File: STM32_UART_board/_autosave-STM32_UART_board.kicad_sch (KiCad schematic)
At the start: 35 parts, among them J1 SWD, J2 Scooter, J3 Conn_01x10, Q1 AO4612_C4748739, SW1 SW_Push, SW2 SW_Push, U1 BAS70-05, U2 LM2574HVM-5, U3 AZ1117-3.3, U4 STM32C011F6Px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

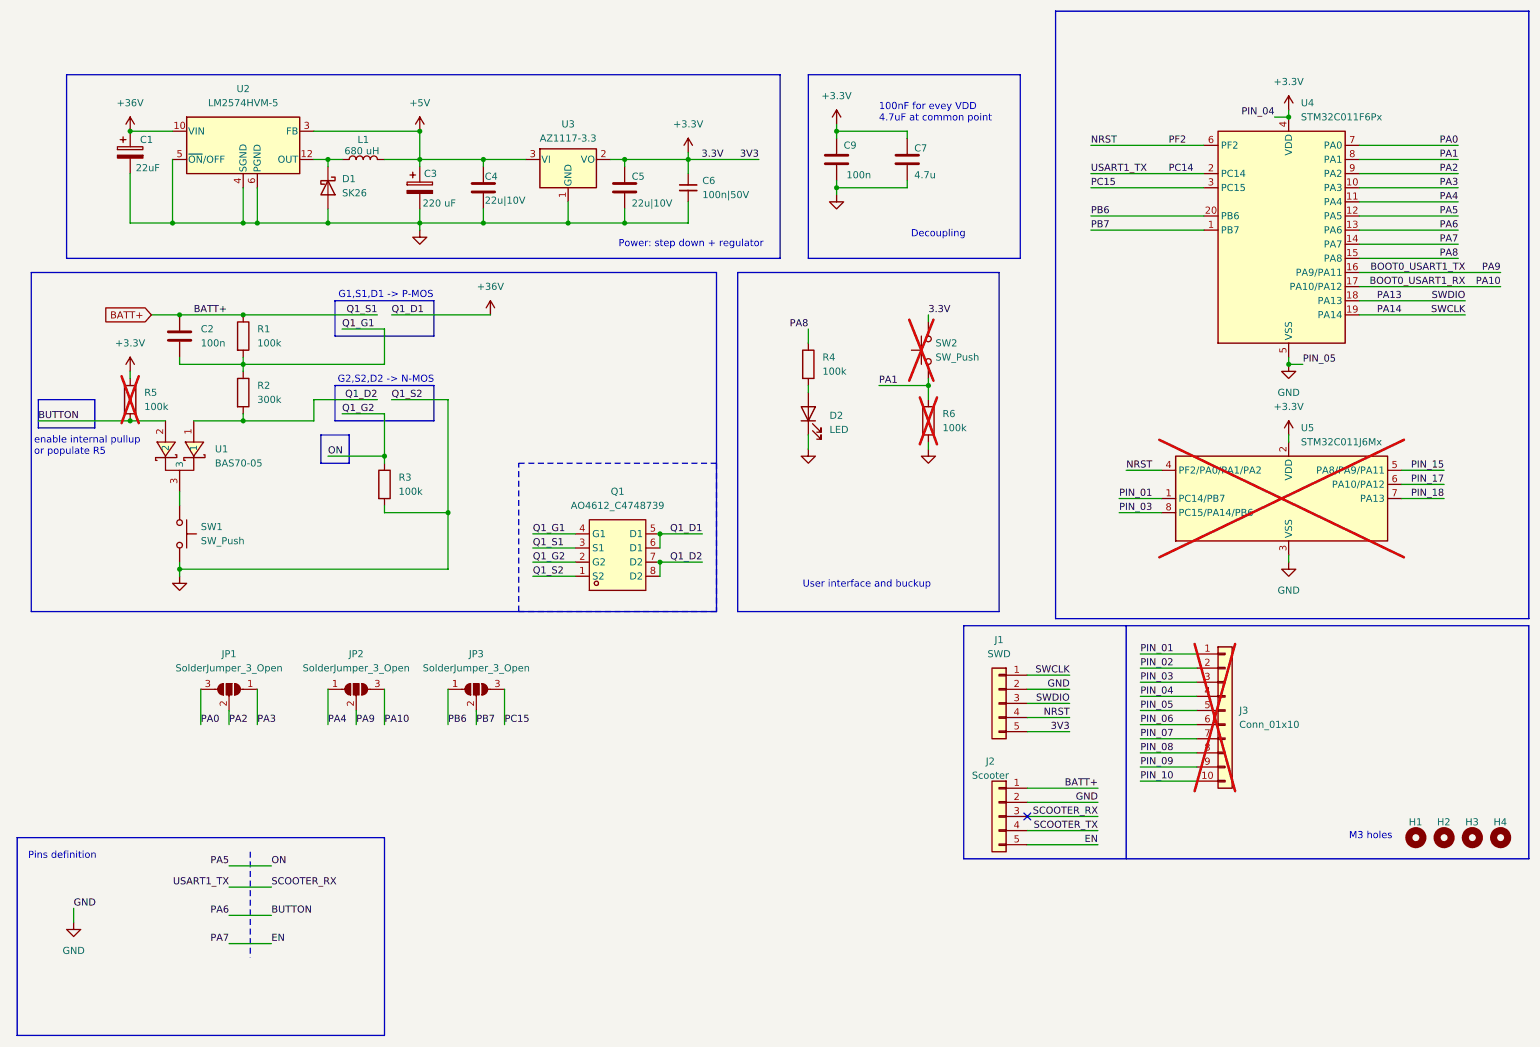
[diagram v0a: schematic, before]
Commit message: PCB with swapped RX TX | initial code fot STM32C011
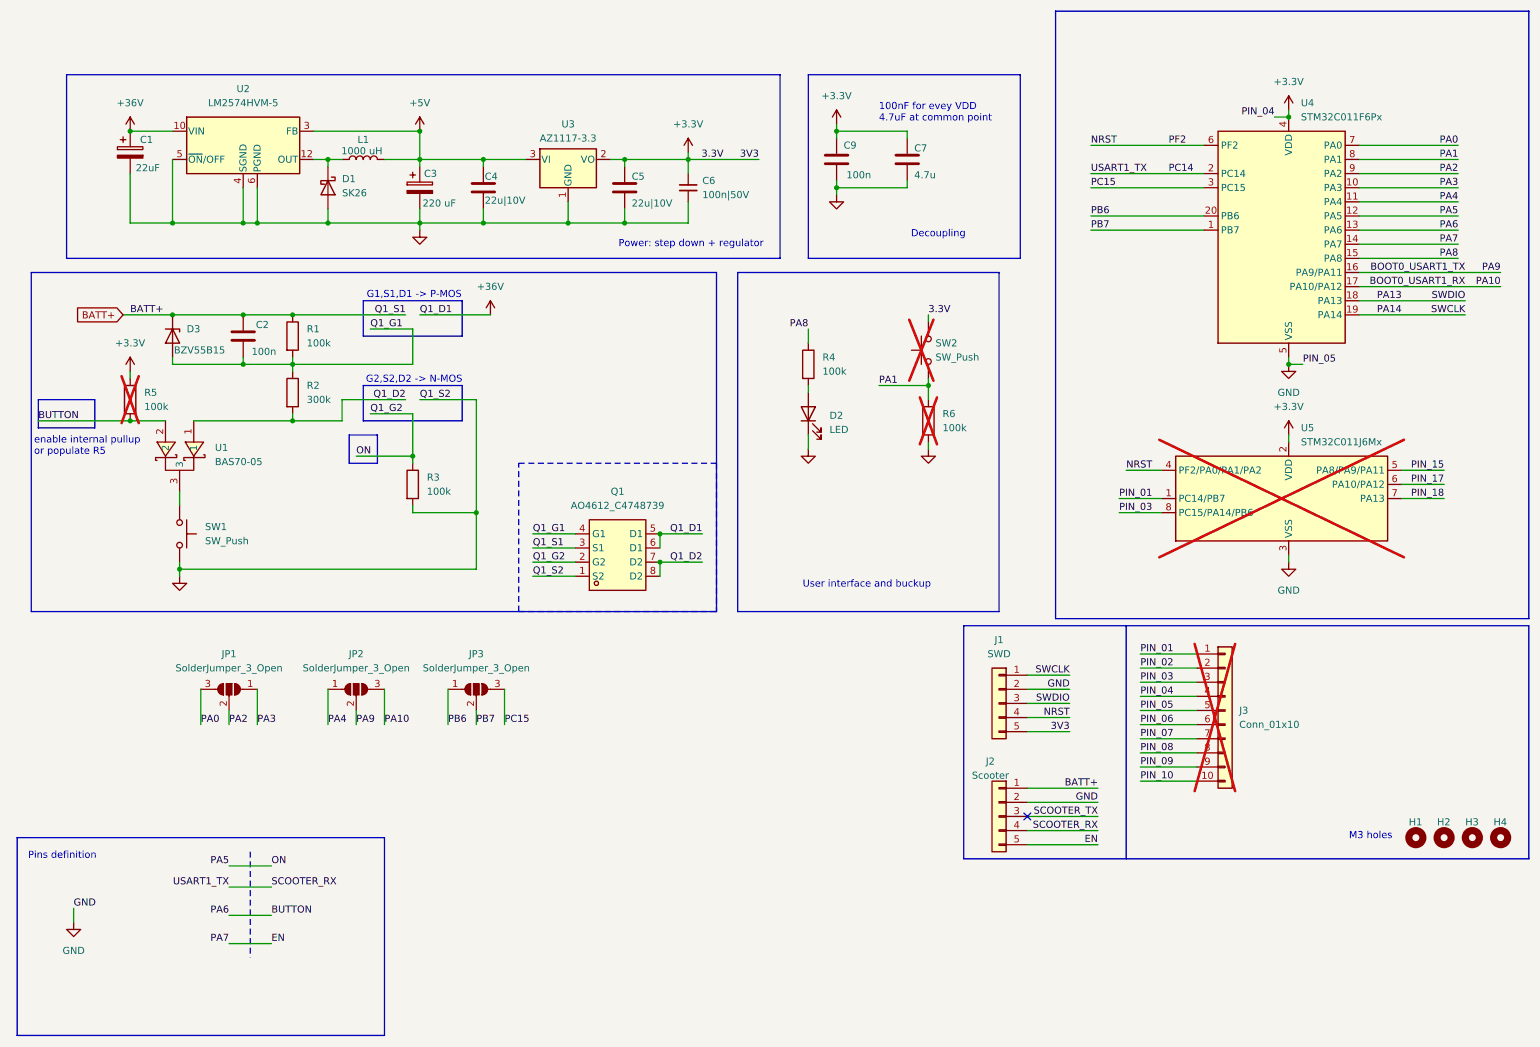
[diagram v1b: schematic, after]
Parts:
- added D3: BZV55B15, Diode_SMD:D_MiniMELF, symbol Diode:BZV55B15
- L1: value 680 uH -> 1000 uH
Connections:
- net BATT+: now also D3.1 (K)
- net PC14: now also J2.4 (Pin_4); no longer J2.3 (Pin_3)
- net Q1_G1: now also D3.2 (A)
- net SCOOTER_TX: now also J2.3 (Pin_3); no longer J2.4 (Pin_4)
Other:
- moved on the sheet: C2, R1, R2, R3
